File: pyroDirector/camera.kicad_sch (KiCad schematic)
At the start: 6 parts, among them J18 Conn_01x03_Male, J19 AudioJack2.5mm, Q2 MMBT2222A 1P, Q3 MMBT2222A 1P

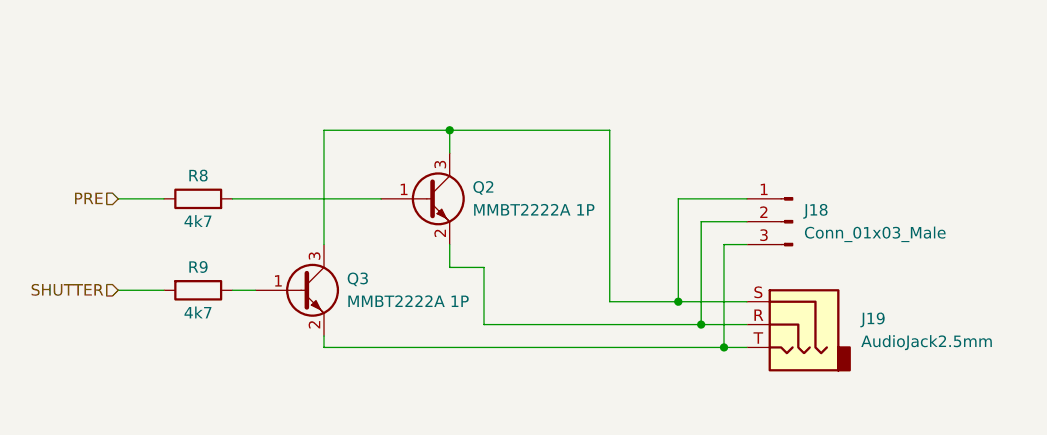
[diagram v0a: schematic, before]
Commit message: Added jacks and PCB switch
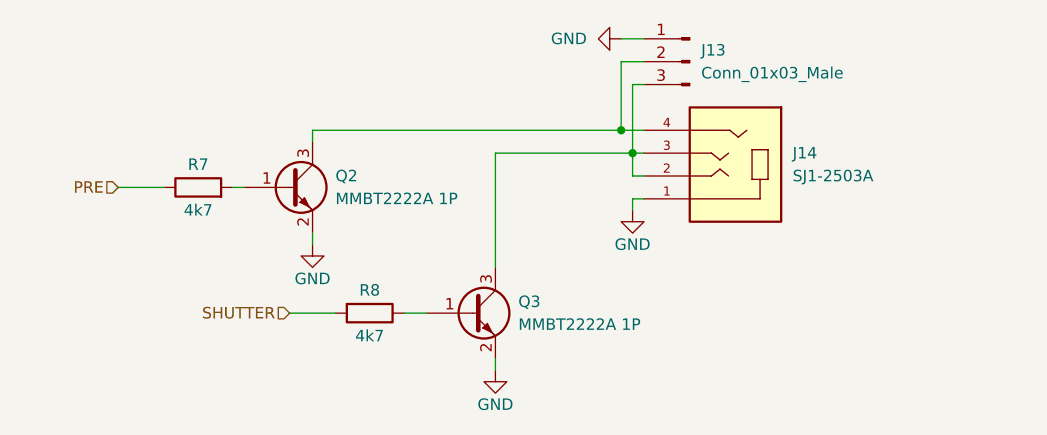
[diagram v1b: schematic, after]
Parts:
- removed J18: Conn_01x03_Male, symbol Connector:Conn_01x03_Male
- removed J19: AudioJack2.5mm, symbol Connector:AudioJack3
- removed R9: 4k7, symbol Device:R
- added J13: Conn_01x03_Male, symbol Connector:Conn_01x03_Male
- added J14: SJ1-2503A, cui-2:CUI_SJ1-2503A, symbol SJ1-2503A:SJ1-2503A
- added R7: 4k7, symbol Device:R
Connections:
- net PRE: now also R7.1; no longer R8.1
- net SHUTTER: now also R8.2
- net GND: now reaches Q2.2 (E)
- net GND: now also Q3.2 (E), J13.1 (Pin_1), J14.1
- net at Q3.3 (C): now also J13.3 (Pin_3), J14.2, J14.3; no longer Q2.3 (C)
- net at Q2.1 (B): now also R7.2; no longer R8.2
- net at Q3.1 (B): now also R8.1
- new net: J13.2 (Pin_2), J14.4, Q2.3 (C)

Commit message: first component placement, trigger header is missing!
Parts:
- J13: footprint (none) -> Connector_PinHeader_2.54mm:PinHeader_1x03_P2.54mm_Vertical
- R7, R8: footprint (none) -> Resistor_SMD:R_0805_2012Metric_Pad1.20x1.40mm_HandSolder
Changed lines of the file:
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@@
     (property "Reference" "R8" (id 0) (at 88.9 68.58 90))
     (property "Value" "4k7" (id 1) (at 88.9 73.66 90))
-    (property "Footprint" "" (id 2) (at 88.9 69.342 90)
+    (property "Footprint" "Resistor_SMD:R_0805_2012Metric_Pad1.20x1.40mm_HandSolder" (id 2) (at 88.9 69.342 90)
       (effects (font (size 1.27 1.27)) hide)
     )
@@
       (effects (font (size 1.27 1.27)) (justify right))
     )
-    (property "Footprint" "" (id 2) (at 124.46 43.18 0)
+    (property "Footprint" "Connector_PinHeader_2.54mm:PinHeader_1x03_P2.54mm_Vertical" (id 2) (at 124.46 43.18 0)
       (effects (font (size 1.27 1.27)) hide)
     )
@@
     (property "Reference" "R7" (id 0) (at 69.85 54.61 90))
     (property "Value" "4k7" (id 1) (at 69.85 59.69 90))
-    (property "Footprint" "" (id 2) (at 69.85 58.928 90)
+    (property "Footprint" "Resistor_SMD:R_0805_2012Metric_Pad1.20x1.40mm_HandSolder" (id 2) (at 69.85 58.928 90)
       (effects (font (size 1.27 1.27)) hide)
     )

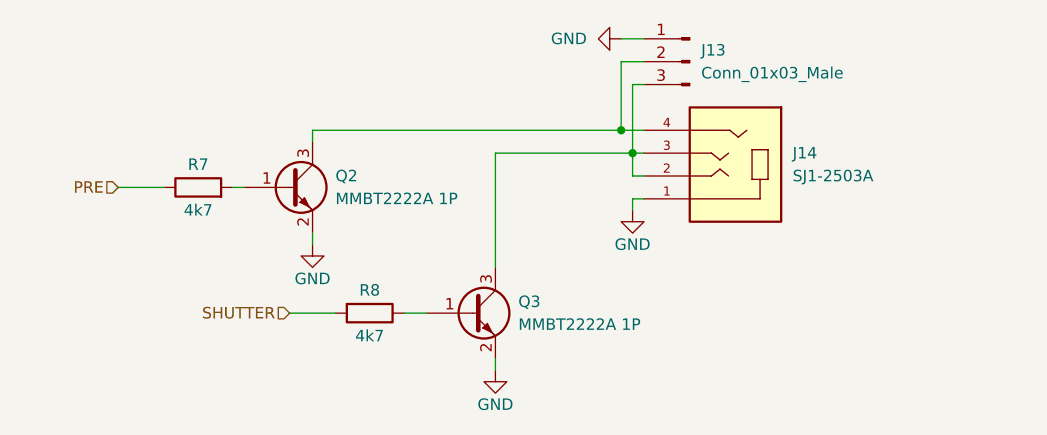
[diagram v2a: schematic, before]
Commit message: placement improvements, added missing header -->should we use handsolder pads?
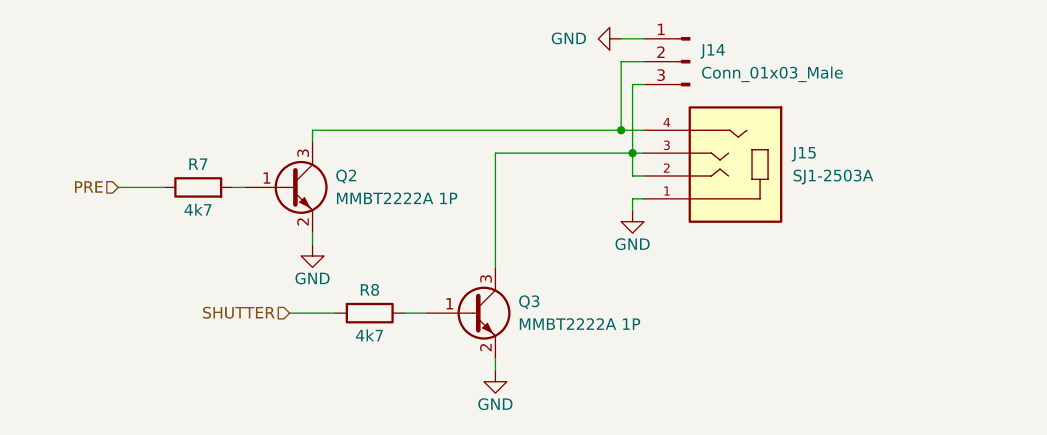
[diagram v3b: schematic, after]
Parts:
- renumbered J13 to J14, J14 to J15
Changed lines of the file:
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@@
   (symbol (lib_id "Connector:Conn_01x03_Male") (at 124.46 43.18 0) (mirror y) (unit 1)
     (in_bom yes) (on_board yes) (fields_autoplaced)
-    (property "Reference" "J13" (id 0) (at 125.73 41.9099 0)
+    (property "Reference" "J14" (id 0) (at 125.73 41.9099 0)
       (effects (font (size 1.27 1.27)) (justify right))
     )
@@
   (symbol (lib_id "SJ1-2503A:SJ1-2503A") (at 129.54 53.34 180) (unit 1)
     (in_bom yes) (on_board yes) (fields_autoplaced)
-    (property "Reference" "J14" (id 0) (at 135.89 53.3399 0)
+    (property "Reference" "J15" (id 0) (at 135.89 53.3399 0)
       (effects (font (size 1.27 1.27)) (justify right))
     )

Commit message: Manufactured 2021-02-25
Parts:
- Q2, Q3: LCSC (none) -> C8512
- R7, R8: LCSC (none) -> C17673
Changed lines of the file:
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@@
+      (effects (font (size 1.27 1.27)) hide)
+    )
+    (property "LCSC" "C17673" (id 4) (at 88.9 71.12 90)
       (effects (font (size 1.27 1.27)) hide)
     )
@@
       (effects (font (size 1.27 1.27)) (justify left) hide)
     )
+    (property "LCSC" "C8512" (id 4) (at 100.33 71.12 0)
+      (effects (font (size 1.27 1.27)) hide)
+    )
     (pin "1")
     (pin "2")
@@
     (property "Datasheet" "https://datasheet.lcsc.com/lcsc/1811081957_Jiangsu-Changjing-Electronics-Technology-Co---Ltd--MMBT2222A-1P_C8512.pdf" (id 3) (at 86.36 60.96 0)
       (effects (font (size 1.27 1.27)) (justify left) hide)
+    )
+    (property "LCSC" "C8512" (id 4) (at 80.01 57.15 0)
+      (effects (font (size 1.27 1.27)) hide)
     )
     (pin "1")
@@
       (effects (font (size 1.27 1.27)) hide)
     )
+    (property "LCSC" "C17673" (id 4) (at 69.85 57.15 90)
+      (effects (font (size 1.27 1.27)) hide)
+    )
